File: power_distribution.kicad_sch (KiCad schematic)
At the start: 0 parts

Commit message: commit
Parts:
- added C1, C2: 10µF, symbol Device:C
- added C3, C4: 100nF, symbol Device:C
- added J1: LiPo_Battery, symbol Connector_Generic:Conn_01x02
- added R1: 100kΩ, symbol Device:R
- added R2: 22kΩ, symbol Device:R
- added U1: AP2112K-3.3, Package_TO_SOT_SMD:SOT-23-5, symbol Regulator_Linear:AP2112K-3.3
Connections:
- new net +3.3V: C2.1, C3.1, U1.5 (VOUT)
- new net +5V: C1.1, U1.1 (VIN), U1.3 (EN)
- new net ESP32_ADC: C4.2, R1.2, R2.1
- new net GND: C1.2, C2.2, C3.2, C4.1, J1.2 (Pin_2), R2.2, U1.2 (GND)
- new net VBAT: J1.1 (Pin_1), R1.1

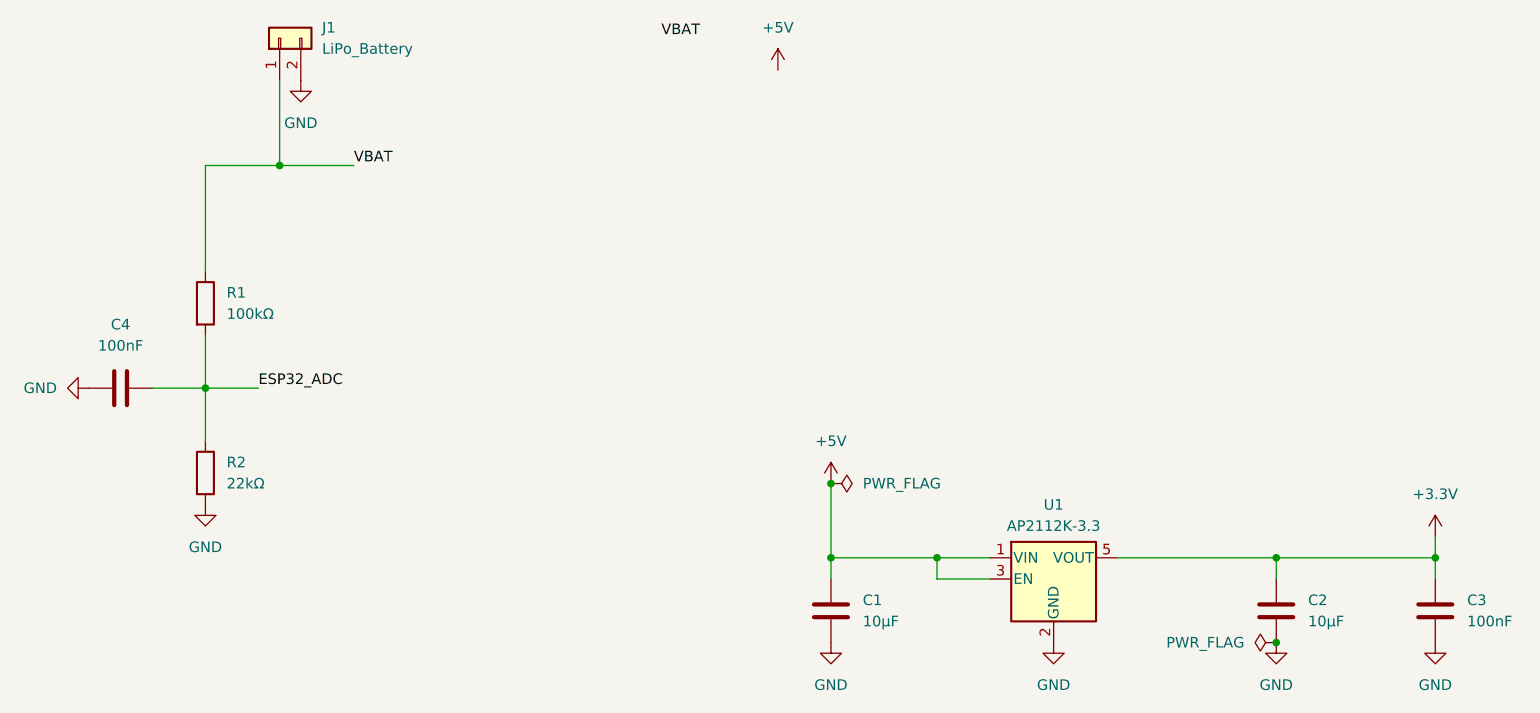
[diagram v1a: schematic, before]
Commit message: Added io_connectors.kicad_sch and power_distribution.kicad_sch, and modified mcu_esp32.kicad_sch
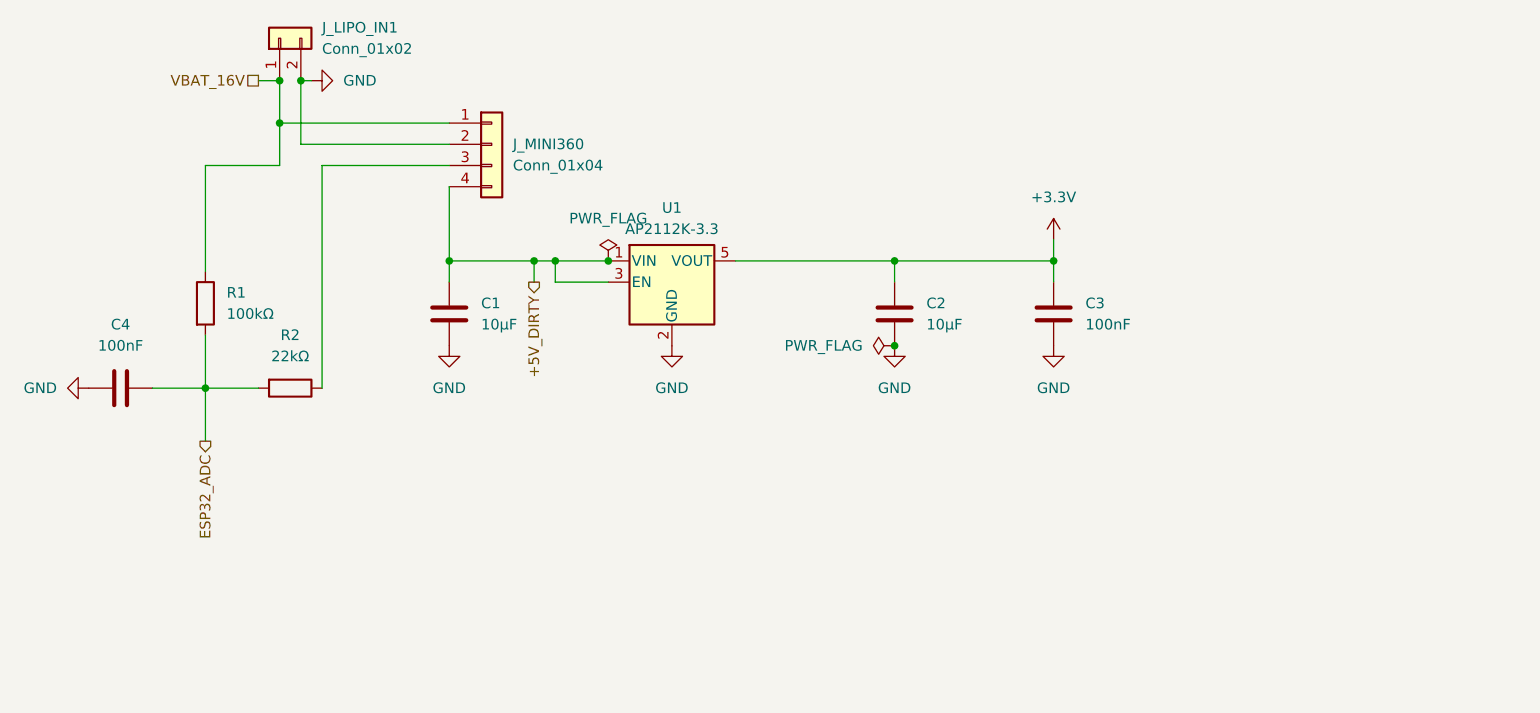
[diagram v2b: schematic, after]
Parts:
- added J_MINI360: Conn_01x04, symbol Connector_Generic:Conn_01x04
- J_LIPO_IN1: renamed from J1; value LiPo_Battery -> Conn_01x02
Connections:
- net ESP32_ADC: now also R2.2; no longer R2.1
- net GND: now also J_MINI360.2 (Pin_2); no longer R2.2
- net +5V renamed +5V_DIRTY
- net +5V_DIRTY: now also J_MINI360.4 (Pin_4)
- net VBAT renamed VBAT_16V
- net VBAT_16V: now also J_MINI360.1 (Pin_1)
- new net: J_MINI360.3 (Pin_3), R2.1
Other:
- moved on the sheet: C1, C2, C3, U1
